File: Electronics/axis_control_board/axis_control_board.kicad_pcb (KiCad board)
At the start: 2 copper layers, 21 parts, among them Q1 S8050, U1 LD33v_TO220, U2 NRF24L01_Breakout, U4 LM7805_TO220

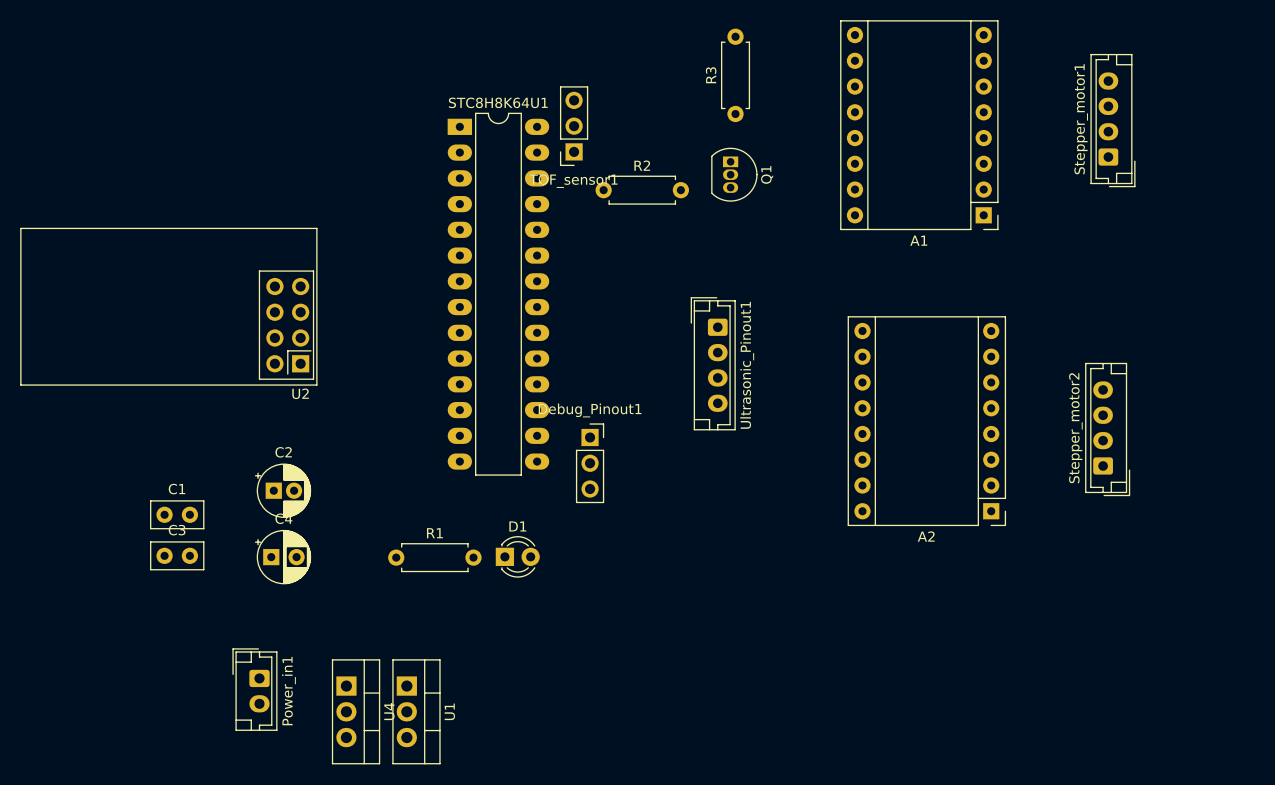
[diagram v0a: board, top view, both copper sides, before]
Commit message: finished axis control PCB design
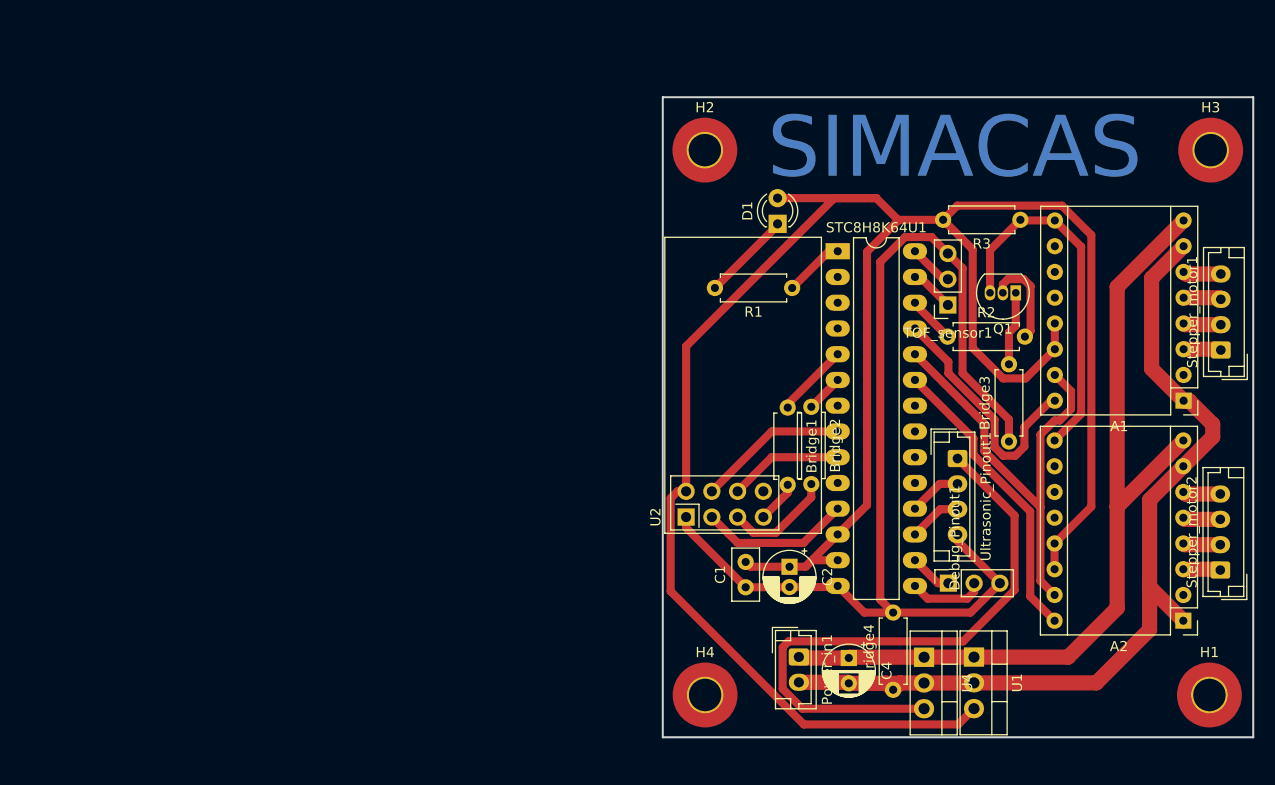
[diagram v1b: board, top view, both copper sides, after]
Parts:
- removed C3: 10nF, Capacitor_THT:C_Disc_D5.0mm_W2.5mm_P2.50mm
- added Bridge1: 0ohm, Resistor_THT:R_Axial_DIN0207_L6.3mm_D2.5mm_P7.62mm_Horizontal, F.Cu at (149.6, 104.2)
- added Bridge2: 0ohm, Resistor_THT:R_Axial_DIN0207_L6.3mm_D2.5mm_P7.62mm_Horizontal, F.Cu at (151.9, 104.2)
- added Bridge3: 0ohm, Resistor_THT:R_Axial_DIN0207_L6.3mm_D2.5mm_P7.62mm_Horizontal, F.Cu at (171.4, 107.6)
- added Bridge4: 0ohm, Resistor_THT:R_Axial_DIN0207_L6.3mm_D2.5mm_P7.62mm_Horizontal, F.Cu at (159.9, 132.1)
- added H1: MountingHole, MountingHole:MountingHole_3.2mm_M3_Pad_TopOnly, F.Cu at (191.2, 132.6)
- added H2: MountingHole, MountingHole:MountingHole_3.2mm_M3_Pad_TopOnly, F.Cu at (141.4, 78.8)
- added H3: MountingHole, MountingHole:MountingHole_3.2mm_M3_Pad_TopOnly, F.Cu at (191.3, 78.8)
- added H4: MountingHole, MountingHole:MountingHole_3.2mm_M3_Pad_TopOnly, F.Cu at (141.4, 132.6)
- R2: value 10k -> 1k
- R3: value 10k -> 220
- moved C4 57.8 mm to (155.6, 128.9), turned to -90 degrees
- moved C1 57.8 mm to (145.4, 122.0), turned to 90 degrees
- moved U4 57.1 mm to (163.0, 128.8)
- moved U1 56.0 mm to (167.9, 128.8)
- moved Power_in1 53.3 mm to (150.7, 128.8)
- moved C2 51.4 mm to (149.7, 119.9), turned to -90 degrees
- moved R1 47.3 mm to (150.0, 92.4), turned to 180 degrees
- moved D1 42.5 mm to (148.6, 86.1), turned to 90 degrees
- moved U2 40.9 mm to (139.5, 115.0), turned to 90 degrees
- moved TOF_sensor1 39.8 mm to (165.3, 94.1)
- moved STC8H8K64U1 39.2 mm to (154.5, 88.8)
- moved Debug_Pinout1 38.2 mm to (165.4, 121.5), turned to 90 degrees
- moved R2 36.9 mm to (165.3, 97.2)
- moved Q1 31.0 mm to (172.0, 92.9), turned to 180 degrees
- moved R3 30.0 mm to (172.5, 85.7), turned to 180 degrees
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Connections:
- D1 pad 2: GND -> +3.3V
- Q1 pad 1: GND -> Net-(Q1-E)
- R1 pad 1: unconnected-(R1-Pad1) -> Net-(STC8H8K64U1-Pin_1)
- STC8H8K64U1 pad 1: CSN -> Net-(STC8H8K64U1-Pin_1)
- STC8H8K64U1 pad 10: Net-(STC8H8K64U1-Pin_10) -> unconnected-(STC8H8K64U1-Pin_10-Pad10)
- STC8H8K64U1 pad 11: unconnected-(STC8H8K64U1-Pin_11-Pad11) -> CE
- STC8H8K64U1 pad 13: unconnected-(STC8H8K64U1-Pin_13-Pad13) -> +3.3V
- STC8H8K64U1 pad 2: CE -> unconnected-(STC8H8K64U1-Pin_2-Pad2)
- STC8H8K64U1 pad 5: MISO -> Net-(STC8H8K64U1-Pin_5)
- STC8H8K64U1 pad 6: SCLK -> Net-(STC8H8K64U1-Pin_6)
- STC8H8K64U1 pad 8: unconnected-(STC8H8K64U1-Pin_8-Pad8) -> CSN
- Stepper_motor1 pad 1: Net-(A1-A1) -> Net-(A1-A2)
- Stepper_motor1 pad 2: Net-(A1-A2) -> Net-(A1-A1)
- Stepper_motor2 pad 1: Net-(A2-A1) -> Net-(A2-A2)
- Stepper_motor2 pad 2: Net-(A2-A2) -> Net-(A2-A1)
- TOF_sensor1 pad 1: SCL -> SDA
- TOF_sensor1 pad 2: SDA -> SCL
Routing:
- net +3.3V: track 0.00 -> 228.7 mm
- net GND: track 0.00 -> 196.2 mm
- net +12V: track 0.00 -> 83.7 mm
- net +5V: track 0.00 -> 59.4 mm
- net STEP: track 0.00 -> 44.7 mm
- net ENABLE_INVERTED: track 0.00 -> 35.7 mm
- net DIR1: track 0.00 -> 29.5 mm
- net DIR2: track 0.00 -> 24.6 mm
- net CE: track 0.00 -> 14.9 mm
- net CSN: track 0.00 -> 14.9 mm
- net MOSI: track 0.00 -> 11.3 mm
- net SCLK: track 0.00 -> 10.7 mm
- net Net-(Q1-B): track 0.00 -> 9.30 mm
- net Net-(D1-K): track 0.00 -> 8.89 mm
- net /RX: track 0.00 -> 7.49 mm
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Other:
- board outline added: 58.2 x 63.2 mm
- board text added: "SIMACAS"
